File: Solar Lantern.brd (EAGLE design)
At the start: 25 x 100 mm, 18 parts, among them Q1 BC557, Q2 BC557, U1 QX5252

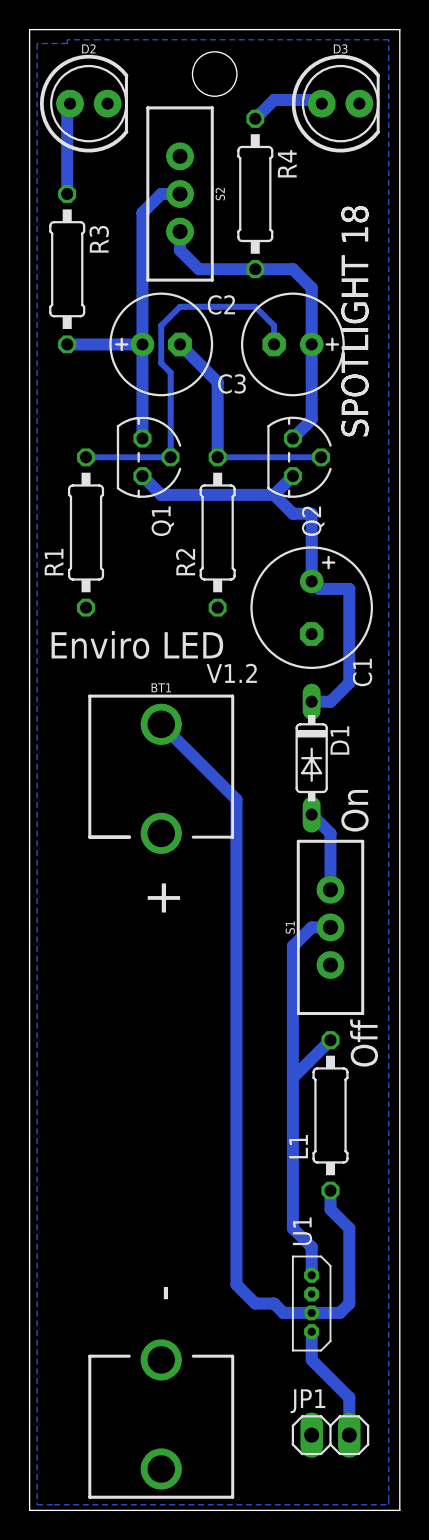
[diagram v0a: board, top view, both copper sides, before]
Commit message: Library Update
changed the package for the QX5252 to make it easier to solder.
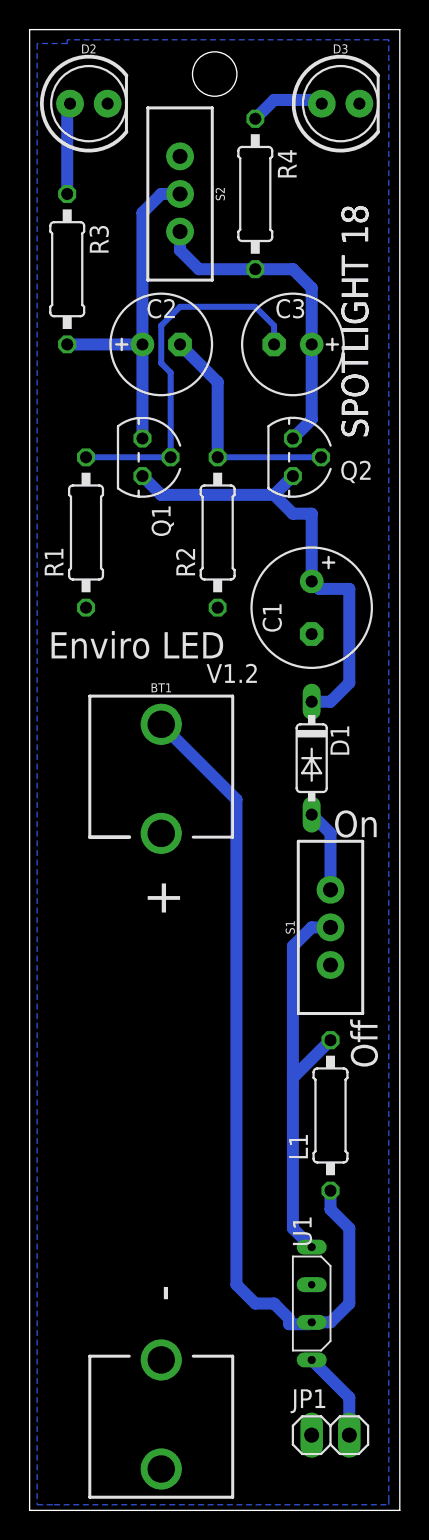
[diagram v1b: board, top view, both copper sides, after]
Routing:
- net N$12: track 29.4 -> 27.5 mm
- net N$10: track 8.04 -> 6.13 mm
- net N$13: track 56.8 -> 57.6 mm
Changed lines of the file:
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@@
 <text x="10.795" y="27.94" size="1.778" layer="22" rot="MR90">SPOTLIGHT 18</text>
 <text x="1.27" y="57.531" size="1.778" layer="21">Enviro LED</text>
-<text x="22.86" y="45.72" size="1.778" layer="21" rot="R90">On</text>
+<text x="23.622" y="47.244" size="1.778" layer="21" rot="R180">On</text>
 <text x="23.495" y="29.845" size="1.778" layer="21" rot="R90">Off</text>
 <rectangle x1="13.5255" y1="23.3045" x2="13.6525" y2="23.4315" layer="200" rot="R270"/>
@@
 <attribute name="SF_SKU" value="PRT-07949" x="8.89" y="27.94" size="1.778" layer="27" rot="R270" display="off"/>
 </element>
-<element name="C1" library="rcl" library_urn="urn:adsk.eagle:library:334" package="E3,5-8" package3d_urn="urn:adsk.eagle:package:23360/2" value="47uF" x="19.05" y="60.96" rot="R270">
+<element name="C1" library="rcl" library_urn="urn:adsk.eagle:library:334" package="E3,5-8" package3d_urn="urn:adsk.eagle:package:23360/2" value="47uF" x="19.05" y="60.96" smashed="yes" rot="R270">
+<attribute name="NAME" x="15.748" y="61.341" size="1.27" layer="25" ratio="10" rot="R270"/>
 <attribute name="SPICEPREFIX" value="C" x="19.05" y="60.96" size="1.778" layer="27" rot="R270" display="off"/>
-</element>
-<element name="C2" library="rcl" library_urn="urn:adsk.eagle:library:334" package="E2,5-7" package3d_urn="urn:adsk.eagle:package:23345/1" value="10uF" x="8.89" y="78.74">
+<attribute name="VALUE" x="20.828" y="62.738" size="1.27" layer="27" ratio="10" rot="R270"/>
+</element>
+<element name="C2" library="rcl" library_urn="urn:adsk.eagle:library:334" package="E2,5-7" package3d_urn="urn:adsk.eagle:package:23345/1" value="10uF" x="8.89" y="78.74" smashed="yes">
+<attribute name="NAME" x="7.874" y="80.518" size="1.27" layer="25" ratio="10"/>
 <attribute name="SPICEPREFIX" value="C" x="8.89" y="78.74" size="1.778" layer="27" display="off"/>
-</element>
-<element name="C3" library="rcl" library_urn="urn:adsk.eagle:library:334" package="E2,5-7" package3d_urn="urn:adsk.eagle:package:23345/1" value="10uF" x="17.78" y="78.74" rot="R180">
+<attribute name="VALUE" x="6.858" y="75.692" size="1.27" layer="27" ratio="10"/>
+</element>
+<element name="C3" library="rcl" library_urn="urn:adsk.eagle:library:334" package="E2,5-7" package3d_urn="urn:adsk.eagle:package:23345/1" value="10uF" x="17.78" y="78.74" smashed="yes" rot="R180">
+<attribute name="NAME" x="18.669" y="81.788" size="1.27" layer="25" ratio="10" rot="R180"/>
 <attribute name="SPICEPREFIX" value="C" x="17.78" y="78.74" size="1.778" layer="27" rot="R180" display="off"/>
-</element>
-<element name="D1" library="diode" library_urn="urn:adsk.eagle:library:210" package="DO35-7" package3d_urn="urn:adsk.eagle:package:43339/1" value="1N5819" x="19.05" y="50.8" rot="R270"/>
+<attribute name="VALUE" x="19.685" y="77.216" size="1.27" layer="27" ratio="10" rot="R180"/>
+</element>
+<element name="D1" library="diode" library_urn="urn:adsk.eagle:library:210" package="DO35-7" package3d_urn="urn:adsk.eagle:package:43339/1" value="1N5819" x="19.05" y="50.8" smashed="yes" rot="R270">
+<attribute name="NAME" x="20.32" y="53.086" size="1.27" layer="25" ratio="10" rot="R270"/>
+<attribute name="VALUE" x="21.844" y="54.483" size="1.27" layer="27" ratio="10" rot="R270"/>
+</element>
 <element name="D2" library="SparkFun-LED" library_urn="urn:adsk.eagle:library:529" package="LED_5MM" package3d_urn="urn:adsk.eagle:package:39353/1" value="White" x="4" y="95"/>
 <element name="D3" library="SparkFun-LED" library_urn="urn:adsk.eagle:library:529" package="LED_5MM" package3d_urn="urn:adsk.eagle:package:39353/1" value="White" x="21" y="95"/>
 <element name="JP1" library="DC_LOAD_AU" library_urn="urn:adsk.eagle:library:220454" package="1X02" package3d_urn="urn:adsk.eagle:package:220539/2" value="Solar" x="20.32" y="5.08"/>
-<element name="L1" library="resistor" library_urn="urn:adsk.eagle:library:348" package="0207/10" package3d_urn="urn:adsk.eagle:package:25939/1" value="100uH" x="20.32" y="26.67" rot="R90"/>
+<element name="L1" library="resistor" library_urn="urn:adsk.eagle:library:348" package="0207/10" package3d_urn="urn:adsk.eagle:package:25939/1" value="100uH" x="20.32" y="26.67" smashed="yes" rot="R90">
+<attribute name="NAME" x="18.796" y="23.622" size="1.27" layer="25" ratio="10" rot="R90"/>
+<attribute name="VALUE" x="20.955" y="24.0284" size="1.27" layer="27" ratio="10" rot="R90"/>
+</element>
 <element name="Q1" library="transistor-pnp" library_urn="urn:adsk.eagle:library:399" package="TO92" package3d_urn="urn:adsk.eagle:package:29211/2" value="BC557" x="7.62" y="71.12" rot="R270"/>
-<element name="Q2" library="transistor-pnp" library_urn="urn:adsk.eagle:library:399" package="TO92" package3d_urn="urn:adsk.eagle:package:29211/2" value="BC557" x="17.78" y="71.12" rot="R270"/>
+<element name="Q2" library="transistor-pnp" library_urn="urn:adsk.eagle:library:399" package="TO92" package3d_urn="urn:adsk.eagle:package:29211/2" value="BC557" x="17.78" y="71.12" smashed="yes" rot="R270">
+<attribute name="NAME" x="20.955" y="69.596" size="1.27" layer="25" ratio="10"/>
+<attribute name="VALUE" x="17.526" y="66.675" size="1.27" layer="27" ratio="10"/>
+</element>
 <element name="R1" library="rcl" library_urn="urn:adsk.eagle:library:334" package="0207/10" package3d_urn="urn:adsk.eagle:package:23491/1" value="150K" x="3.81" y="66.04" rot="R90">
 <attribute name="SPICEPREFIX" value="R" x="3.81" y="66.04" size="1.778" layer="27" rot="R90" display="off"/>
@@
 <attribute name="SF_SKU" value="COM-00102" x="10.16" y="88.9" size="1.778" layer="27" rot="R180" display="off"/>
 </element>
-<element name="U1" library="Alicad" package="TO94" value="QX5252" x="19.05" y="13.97" rot="R90"/>
+<element name="U1" library="Alicad" package="TO94" value="QX5252" x="19.05" y="13.97" smashed="yes" rot="R90">
+<attribute name="NAME" x="19.05" y="17.78" size="1.27" layer="25" rot="R90"/>
+<attribute name="VALUE" x="21.971" y="12.7" size="1.016" layer="27" rot="R90"/>
+</element>
 </elements>
 <signals>
@@
 <contactref element="JP1" pad="2"/>
 <contactref element="U1" pad="1"/>
-<wire x1="19.05" y1="12.065" x2="19.05" y2="10.16" width="0.8128" layer="16"/>
-<wire x1="19.05" y1="10.16" x2="21.59" y2="7.62" width="0.8128" layer="16"/>
-<wire x1="21.59" y1="7.62" x2="21.59" y2="5.08" width="0.8128" layer="16"/>
+<wire x1="21.59" y1="5.08" x2="21.59" y2="7.62" width="0.8128" layer="16"/>
+<wire x1="21.59" y1="7.62" x2="19.05" y2="10.16" width="0.8128" layer="16"/>
 </signal>
 <signal name="N$12">
@@
 <contactref element="S1" pad="2"/>
 <contactref element="L1" pad="2"/>
-<wire x1="19.05" y1="15.875" x2="19.05" y2="17.78" width="0.8128" layer="16"/>
-<wire x1="19.05" y1="17.78" x2="17.78" y2="19.05" width="0.8128" layer="16"/>
-<wire x1="17.78" y1="19.05" x2="17.78" y2="29.21" width="0.8128" layer="16"/>
+<wire x1="17.78" y1="29.21" x2="17.78" y2="19.05" width="0.8128" layer="16"/>
 <wire x1="17.78" y1="29.21" x2="20.32" y2="31.75" width="0.8128" layer="16"/>
 <wire x1="20.32" y1="39.37" x2="19.05" y2="39.37" width="0.8128" layer="16"/>
 <wire x1="19.05" y1="39.37" x2="17.78" y2="38.1" width="0.8128" layer="16"/>
 <wire x1="17.78" y1="38.1" x2="17.78" y2="29.21" width="0.8128" layer="16"/>
+<wire x1="17.78" y1="19.05" x2="19.05" y2="17.78" width="0.8128" layer="16"/>
 </signal>
 <signal name="N$13">
@@
 <contactref element="BT1" pad="PWR@1"/>
 <contactref element="U1" pad="2"/>
-<wire x1="19.05" y1="13.335" x2="20.955" y2="13.335" width="0.8128" layer="16"/>
-<wire x1="20.955" y1="13.335" x2="21.59" y2="13.97" width="0.8128" layer="16"/>
 <wire x1="21.59" y1="13.97" x2="21.59" y2="19.05" width="0.8128" layer="16"/>
 <wire x1="21.59" y1="19.05" x2="20.32" y2="20.32" width="0.8128" layer="16"/>
@@
 <wire x1="13.97" y1="48.006" x2="13.97" y2="15.24" width="0.8128" layer="16"/>
 <wire x1="13.97" y1="15.24" x2="15.24" y2="13.97" width="0.8128" layer="16"/>
-<wire x1="16.51" y1="13.97" x2="15.24" y2="13.97" width="0.8128" layer="16"/>
-<wire x1="19.05" y1="13.335" x2="17.145" y2="13.335" width="0.8128" layer="16"/>
-<wire x1="17.145" y1="13.335" x2="16.51" y2="13.97" width="0.8128" layer="16"/>
+<wire x1="15.24" y1="13.97" x2="16.51" y2="13.97" width="0.8128" layer="16"/>
+<wire x1="16.51" y1="13.97" x2="17.526" y2="12.954" width="0.8128" layer="16"/>
+<wire x1="17.526" y1="12.954" x2="17.526" y2="12.573" width="0.8128" layer="16"/>
+<wire x1="17.526" y1="12.573" x2="18.923" y2="12.573" width="0.8128" layer="16"/>
+<wire x1="18.923" y1="12.573" x2="19.05" y2="12.7" width="0.8128" layer="16"/>
+<wire x1="19.05" y1="12.7" x2="20.32" y2="12.7" width="0.8128" layer="16"/>
+<wire x1="20.32" y1="12.7" x2="21.59" y2="13.97" width="0.8128" layer="16"/>
 </signal>
 <signal name="N$14">
